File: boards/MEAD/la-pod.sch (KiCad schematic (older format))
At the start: 4 parts, among them J1 CONN_SFF8087

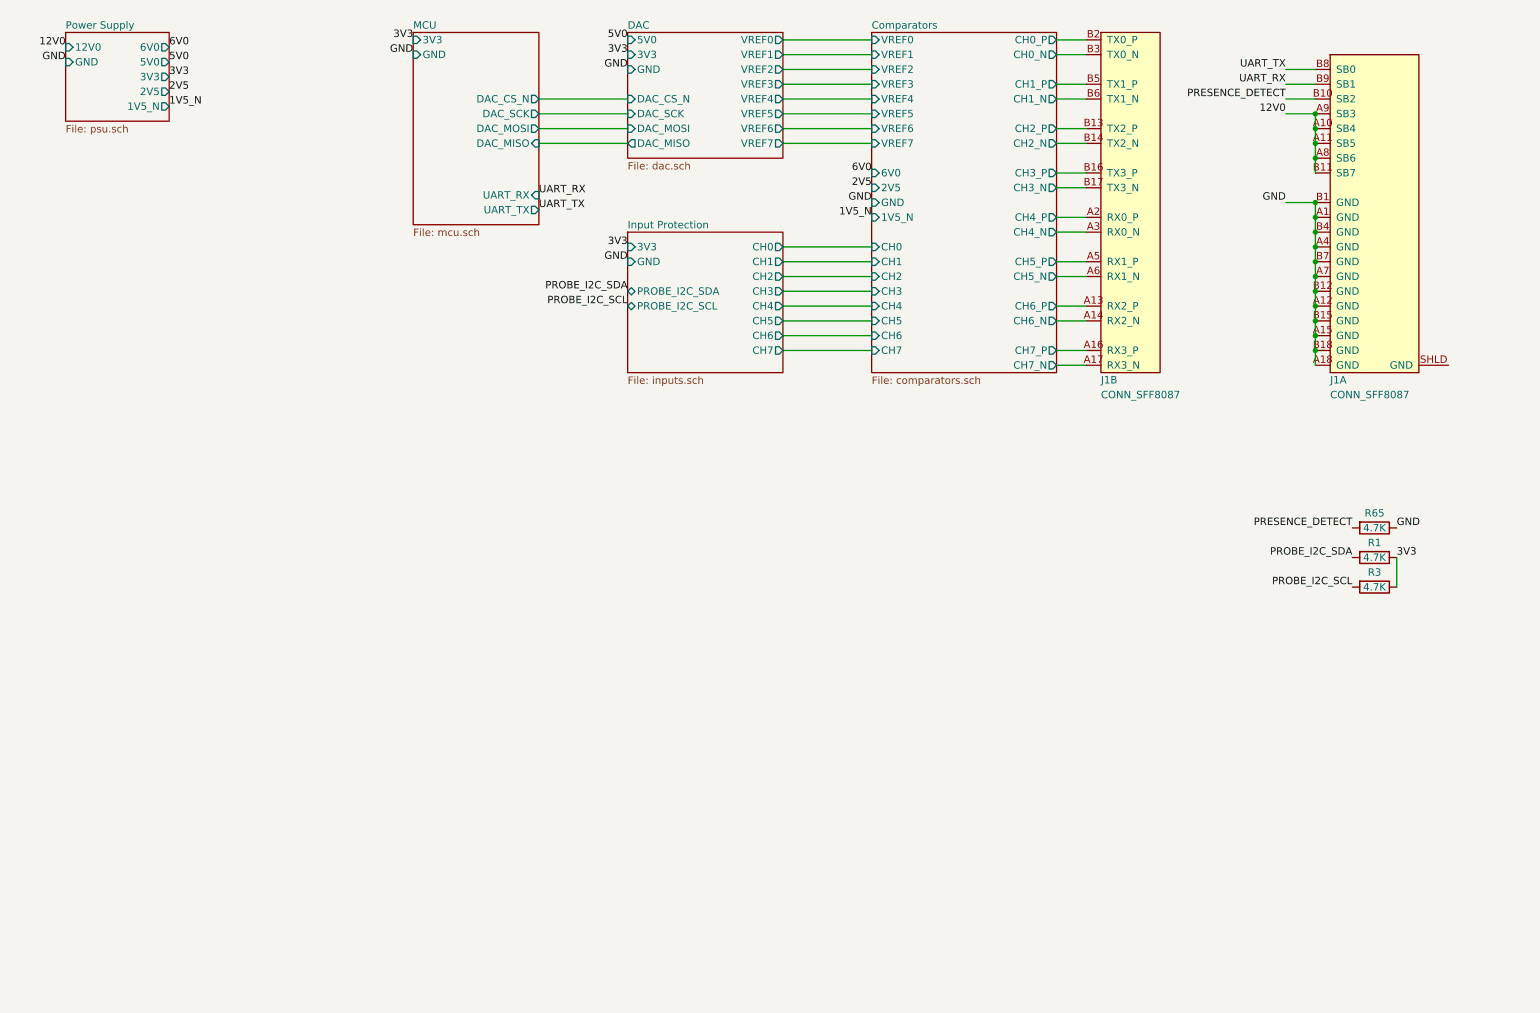
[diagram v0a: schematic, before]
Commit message: Updated MEAD LA pod design with display and different protection diodes
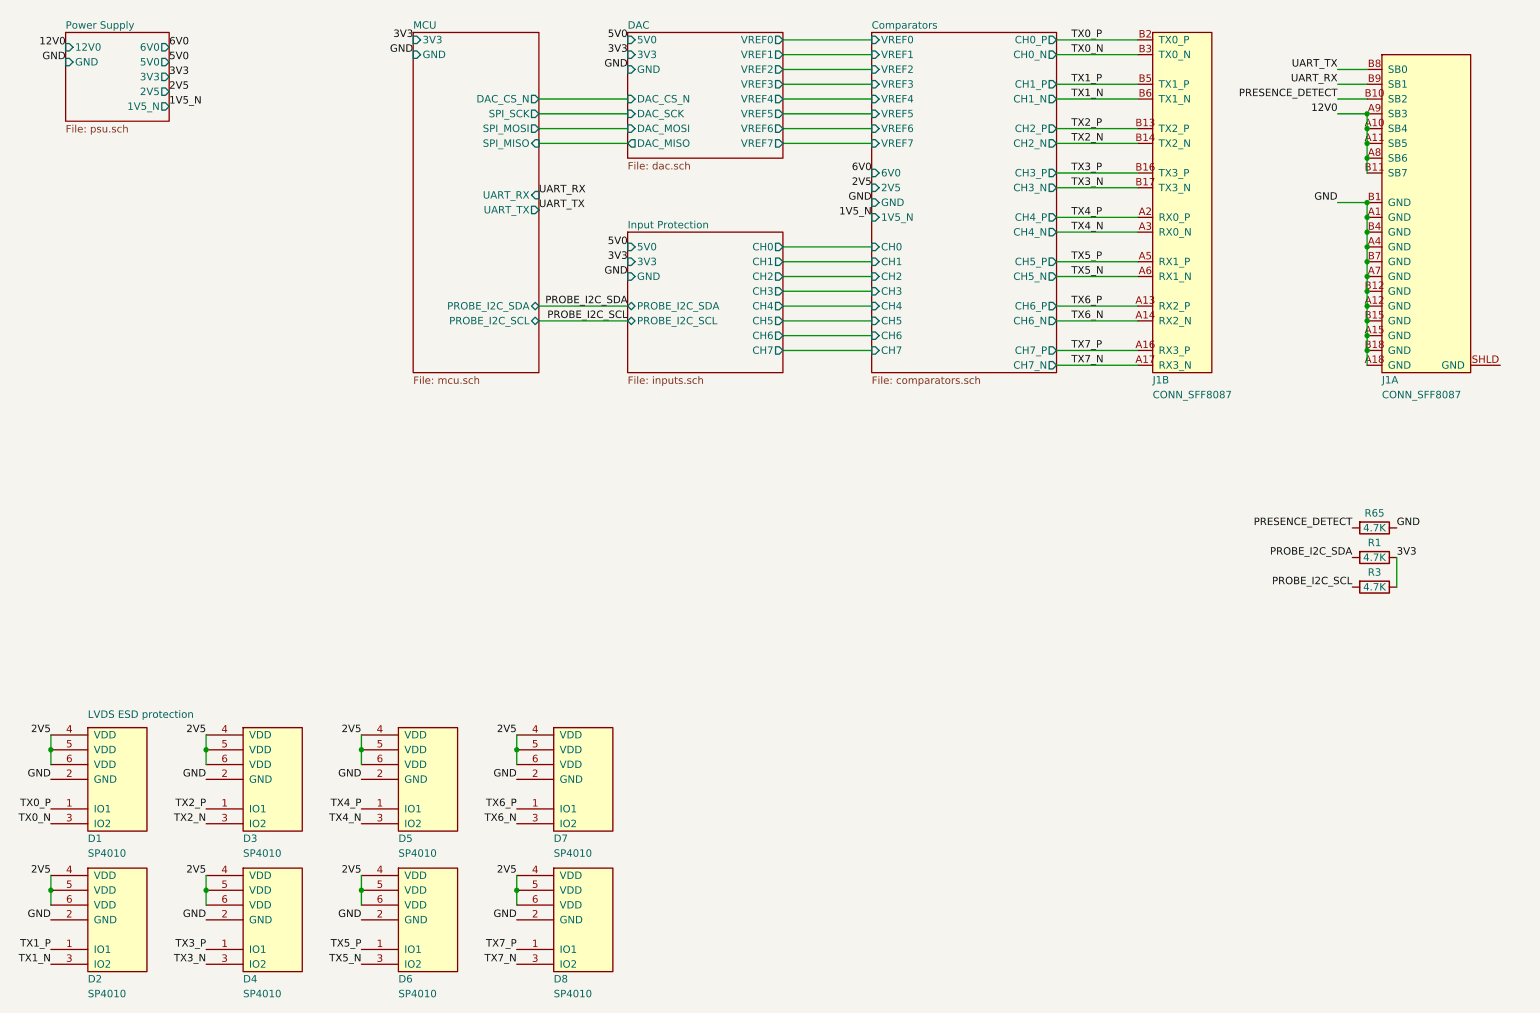
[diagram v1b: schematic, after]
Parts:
- added D1, D2, D3, D4, D5, D6, D7, D8: SP4010, symbol special-azonenberg:SP4010
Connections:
- net 2V5: now also D1.4 (VDD), D1.5 (VDD), D1.6 (VDD), D2.4 (VDD), D2.5 (VDD), D2.6 (VDD), D3.4 (VDD), D3.5 (VDD), D3.6 (VDD), D4.4 (VDD), D4.5 (VDD), D4.6 (VDD), D5.4 (VDD), D5.5 (VDD), D5.6 (VDD), D6.4 (VDD), D6.5 (VDD), D6.6 (VDD), D7.4 (VDD), D7.5 (VDD), D7.6 (VDD), D8.4 (VDD), D8.5 (VDD), D8.6 (VDD)
- net GND: now also D1.2 (GND), D2.2 (GND), D3.2 (GND), D4.2 (GND), D5.2 (GND), D6.2 (GND), D7.2 (GND), D8.2 (GND)
- net Comparators/CH0_N renamed TX0_N
- net TX0_N: now also D1.3 (IO2)
- net Comparators/CH0_P renamed TX0_P
- net TX0_P: now also D1.1 (IO1)
- net Comparators/CH1_N renamed TX1_N
- net TX1_N: now also D2.3 (IO2)
- net Comparators/CH1_P renamed TX1_P
- net TX1_P: now also D2.1 (IO1)
- net Comparators/CH2_N renamed TX2_N
- net TX2_N: now also D3.3 (IO2)
- net Comparators/CH2_P renamed TX2_P
- net TX2_P: now also D3.1 (IO1)
- net Comparators/CH3_N renamed TX3_N
- net TX3_N: now also D4.3 (IO2)
- net Comparators/CH3_P renamed TX3_P
- net TX3_P: now also D4.1 (IO1)
- net Comparators/CH4_N renamed TX4_N
- net TX4_N: now also D5.3 (IO2)
- net Comparators/CH4_P renamed TX4_P
- net TX4_P: now also D5.1 (IO1)
- net Comparators/CH5_N renamed TX5_N
- net TX5_N: now also D6.3 (IO2)
- net Comparators/CH5_P renamed TX5_P
- net TX5_P: now also D6.1 (IO1)
- net Comparators/CH6_N renamed TX6_N
- net TX6_N: now also D7.3 (IO2)
- net Comparators/CH6_P renamed TX6_P
- net TX6_P: now also D7.1 (IO1)
- net Comparators/CH7_N renamed TX7_N
- net TX7_N: now also D8.3 (IO2)
- net Comparators/CH7_P renamed TX7_P
- net TX7_P: now also D8.1 (IO1)
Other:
- note added: "LVDS ESD protection"
- moved on the sheet: J1A, J1B

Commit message: Updated LA pod schematic with additional ESD protection and noise filtering
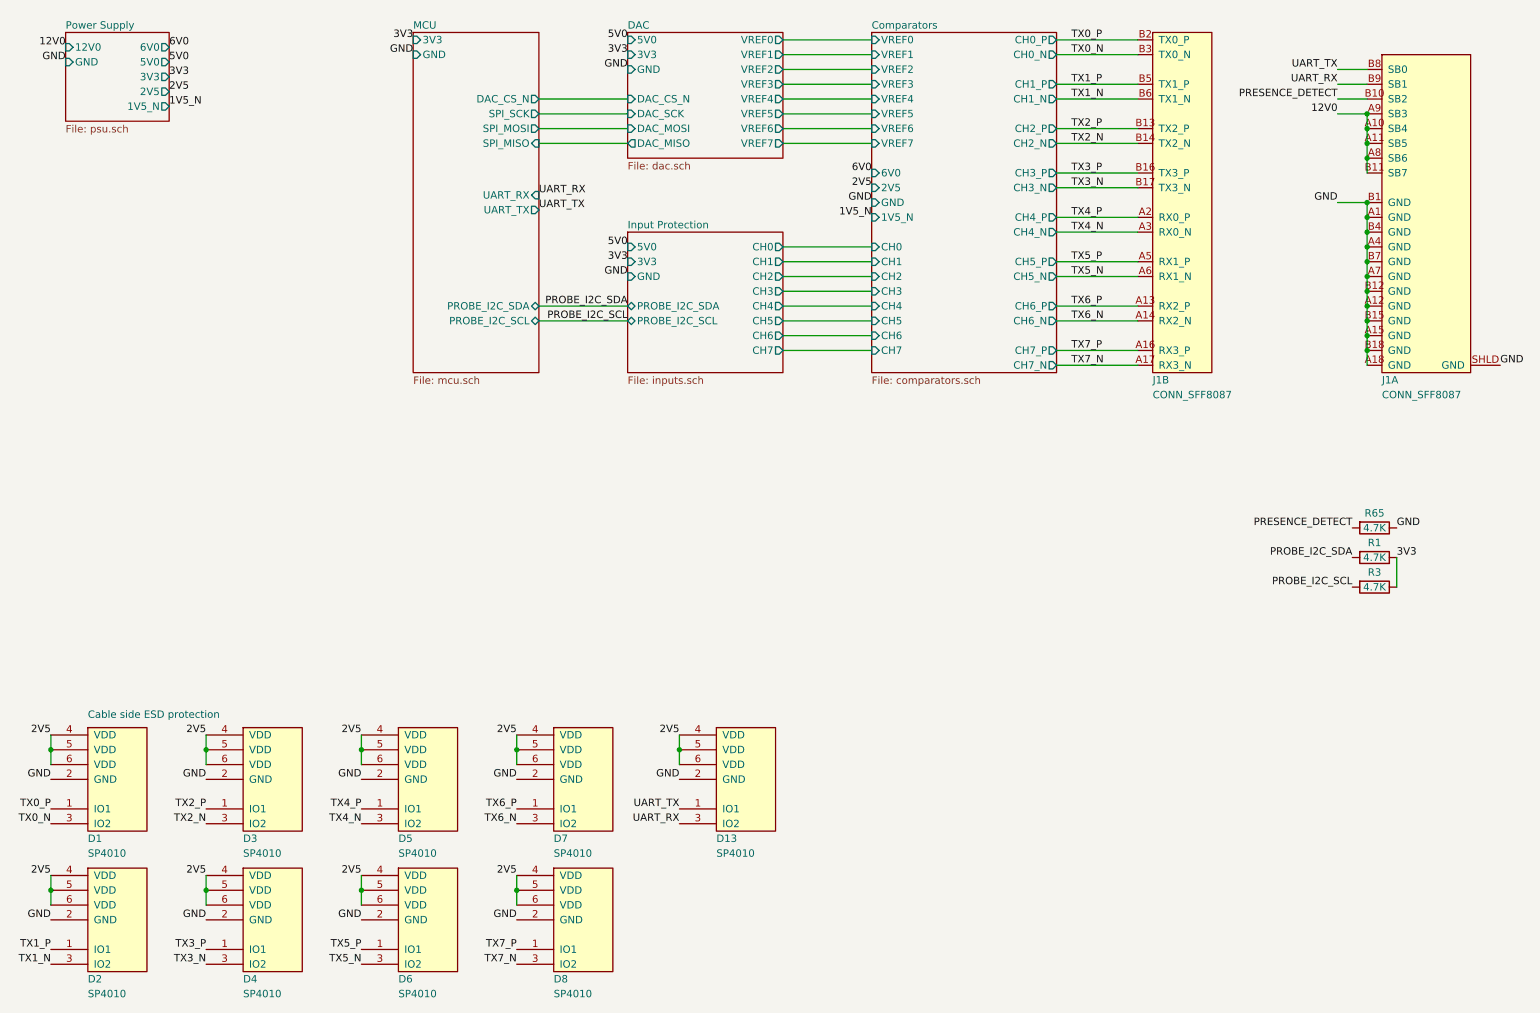
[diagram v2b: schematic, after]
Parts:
- added D13: SP4010, azonenberg_pcb:SOT23_6, symbol special-azonenberg:SP4010
- D1, D2, D3, D4, D5, D6, D7, D8: footprint (none) -> azonenberg_pcb:SOT23_6
- J1: footprint (none) -> azonenberg_pcb:CONN_SFF8087_MOLEX_75783-0140
- R1, R3, R65: footprint (none) -> azonenberg_pcb:EIA_0402_RES_NOSILK
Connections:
- net 2V5: now also D13.4 (VDD), D13.5 (VDD), D13.6 (VDD)
- net GND: now also J1.SHLD (GND), D13.2 (GND)
- net UART_RX: now also D13.3 (IO2)
- net UART_TX: now also D13.1 (IO1)
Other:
- note added: "Cable side ESD protection"
- note removed: "LVDS ESD protection"
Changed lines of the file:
@@
 F 0 "J1" H 9900 3400 50  0000 L CNN
 F 1 "CONN_SFF8087" H 9900 3300 50  0000 L CNN
-F 2 "" H 9900 3450 50  0001 C CNN
+F 2 "azonenberg_pcb:CONN_SFF8087_MOLEX_75783-0140" H 9900 3450 50  0001 C CNN
 F 3 "" H 9900 3450 50  0001 C CNN
 	1    9900 3450
@@
 F 0 "J1" H 8350 3400 50  0000 L CNN
 F 1 "CONN_SFF8087" H 8350 3300 50  0000 L CNN
-F 2 "" H 8350 3450 50  0001 C CNN
+F 2 "azonenberg_pcb:CONN_SFF8087_MOLEX_75783-0140" H 8350 3450 50  0001 C CNN
 F 3 "" H 8350 3450 50  0001 C CNN
 	2    8350 3450
@@
 F 0 "R65" V 9750 4500 50  0000 C CNN
 F 1 "4.7K" V 9850 4500 50  0000 C CNN
-F 2 "" V 9780 4500 50  0001 C CNN
+F 2 "azonenberg_pcb:EIA_0402_RES_NOSILK" V 9780 4500 50  0001 C CNN
 F 3 "" H 9850 4500 50  0001 C CNN
 	1    9850 4500
@@
 F 0 "R1" V 9750 4700 50  0000 C CNN
 F 1 "4.7K" V 9850 4700 50  0000 C CNN
-F 2 "" V 9780 4700 50  0001 C CNN
+F 2 "azonenberg_pcb:EIA_0402_RES_NOSILK" V 9780 4700 50  0001 C CNN
 F 3 "" H 9850 4700 50  0001 C CNN
 	1    9850 4700
@@
 F 0 "R3" V 9750 4900 50  0000 C CNN
 F 1 "4.7K" V 9850 4900 50  0000 C CNN
-F 2 "" V 9780 4900 50  0001 C CNN
+F 2 "azonenberg_pcb:EIA_0402_RES_NOSILK" V 9780 4900 50  0001 C CNN
 F 3 "" H 9850 4900 50  0001 C CNN
 	1    9850 4900
@@
 F 0 "D1" H 1150 6500 50  0000 L CNN
 F 1 "SP4010" H 1150 6400 50  0000 L CNN
-F 2 "" H 1150 6550 50  0001 C CNN
+F 2 "azonenberg_pcb:SOT23_6" H 1150 6550 50  0001 C CNN
 F 3 "" H 1150 6550 50  0001 C CNN
 	1    1150 6550
@@
 F 0 "D2" H 1150 7450 50  0000 L CNN
 F 1 "SP4010" H 1150 7350 50  0000 L CNN
-F 2 "" H 1150 7500 50  0001 C CNN
+F 2 "azonenberg_pcb:SOT23_6" H 1150 7500 50  0001 C CNN
 F 3 "" H 1150 7500 50  0001 C CNN
 	1    1150 7500
@@
 GND
 Text Notes 1150 5800 0    50   ~ 0
-LVDS ESD protection
+Cable side ESD protection
 $Comp
 L special-azonenberg:SP4010 D3
@@
 F 0 "D3" H 2200 6500 50  0000 L CNN
 F 1 "SP4010" H 2200 6400 50  0000 L CNN
-F 2 "" H 2200 6550 50  0001 C CNN
+F 2 "azonenberg_pcb:SOT23_6" H 2200 6550 50  0001 C CNN
 F 3 "" H 2200 6550 50  0001 C CNN
 	1    2200 6550
@@
 F 0 "D4" H 2200 7450 50  0000 L CNN
 F 1 "SP4010" H 2200 7350 50  0000 L CNN
-F 2 "" H 2200 7500 50  0001 C CNN
+F 2 "azonenberg_pcb:SOT23_6" H 2200 7500 50  0001 C CNN
 F 3 "" H 2200 7500 50  0001 C CNN
 	1    2200 7500
@@
 F 0 "D5" H 3250 6500 50  0000 L CNN
 F 1 "SP4010" H 3250 6400 50  0000 L CNN
-F 2 "" H 3250 6550 50  0001 C CNN
+F 2 "azonenberg_pcb:SOT23_6" H 3250 6550 50  0001 C CNN
 F 3 "" H 3250 6550 50  0001 C CNN
 	1    3250 6550
@@
 F 0 "D6" H 3250 7450 50  0000 L CNN
 F 1 "SP4010" H 3250 7350 50  0000 L CNN
-F 2 "" H 3250 7500 50  0001 C CNN
+F 2 "azonenberg_pcb:SOT23_6" H 3250 7500 50  0001 C CNN
 F 3 "" H 3250 7500 50  0001 C CNN
 	1    3250 7500
@@
 F 0 "D7" H 4300 6500 50  0000 L CNN
 F 1 "SP4010" H 4300 6400 50  0000 L CNN
-F 2 "" H 4300 6550 50  0001 C CNN
+F 2 "azonenberg_pcb:SOT23_6" H 4300 6550 50  0001 C CNN
 F 3 "" H 4300 6550 50  0001 C CNN
 	1    4300 6550
@@
 F 0 "D8" H 4300 7450 50  0000 L CNN
 F 1 "SP4010" H 4300 7350 50  0000 L CNN
-F 2 "" H 4300 7500 50  0001 C CNN
+F 2 "azonenberg_pcb:SOT23_6" H 4300 7500 50  0001 C CNN
 F 3 "" H 4300 7500 50  0001 C CNN
 	1    4300 7500
@@
 Wire Wire Line
 	4200 3100 4800 3100
+Text Label 10700 3400 0    50   ~ 0
+GND
+$Comp
+L special-azonenberg:SP4010 D13
+U 1 1 5ED20175
+P 5400 6550
+F 0 "D13" H 5400 6500 50  0000 L CNN
+F 1 "SP4010" H 5400 6400 50  0000 L CNN
+F 2 "azonenberg_pcb:SOT23_6" H 5400 6550 50  0001 C CNN
+F 3 "" H 5400 6550 50  0001 C CNN
+	1    5400 6550
+	1    0    0    -1
+$EndComp
+Text Label 5150 5900 2    50   ~ 0
+2V5
+Wire Wire Line
+	5150 5900 5150 6000
+Connection ~ 5150 6000
+Wire Wire Line
+	5150 6000 5150 6100
+Text Label 5150 6200 2    50   ~ 0
+GND
+Text Label 5150 6400 2    50   ~ 0
+UART_TX
+Text Label 5150 6500 2    50   ~ 0
+UART_RX
 $EndSCHEMATC

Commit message: MEAD: finished schematic review, added more test points
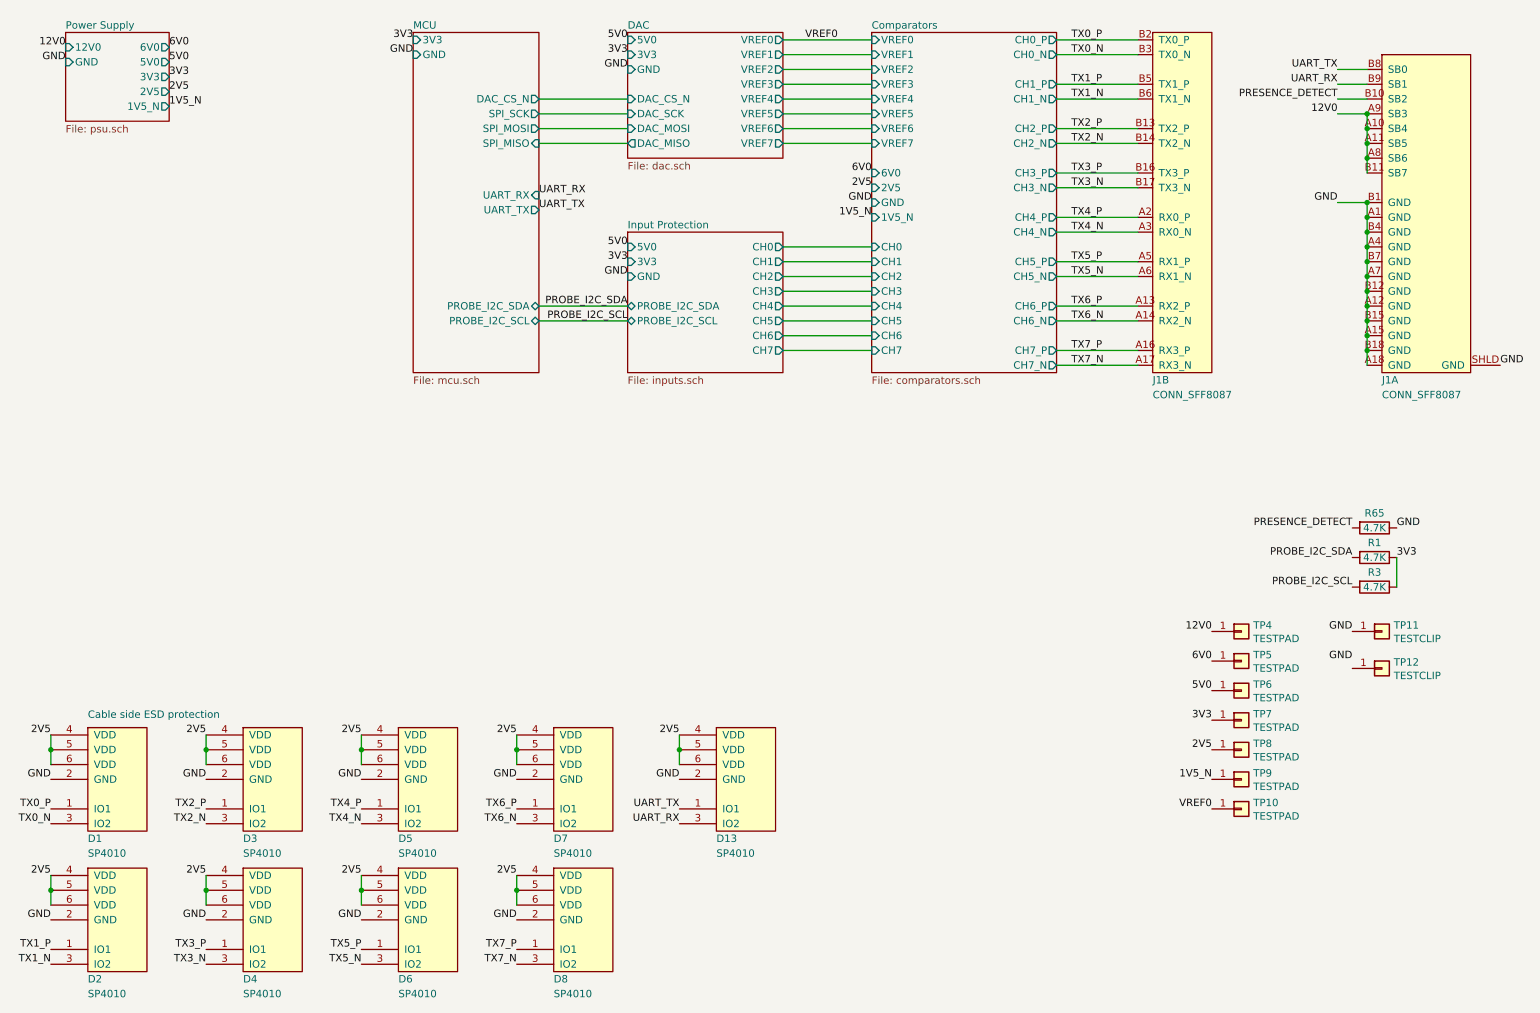
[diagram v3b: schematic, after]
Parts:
- added TP10, TP4, TP5, TP6, TP7, TP8, TP9: TESTPAD, azonenberg_pcb:TESTPOINT_SMT_0.5MM, symbol Connector:Conn_01x01
- added TP11, TP12: TESTCLIP, azonenberg_pcb:TESTPOINT_SMT_KEYSTONE_5016, symbol Connector:Conn_01x01
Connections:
- net 12V0: now also TP4.1 (Pin_1)
- net 1V5_N: now also TP9.1 (Pin_1)
- net 2V5: now also TP8.1 (Pin_1)
- net 3V3: now also TP7.1 (Pin_1)
- net 5V0: now also TP6.1 (Pin_1)
- net 6V0: now also TP5.1 (Pin_1)
- net GND: now also TP11.1 (Pin_1)
- new net VREF0: TP10.1 (Pin_1)
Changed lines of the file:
@@
 Sheet 1 6
 Title "Logic Analyzer Pod"
-Date "2020-05-28"
+Date "2020-05-29"
 Rev "0.1"
 Comp "Antikernel Labs"
@@
 Text Label 5150 6500 2    50   ~ 0
 UART_RX
+$Comp
+L Connector:Conn_01x01 TP11
+U 1 1 5ED596F2
+P 9900 5200
+F 0 "TP11" H 9980 5242 50  0000 L CNN
+F 1 "TESTCLIP" H 9980 5151 50  0000 L CNN
+F 2 "azonenberg_pcb:TESTPOINT_SMT_KEYSTONE_5016" H 9900 5200 50  0001 C CNN
+F 3 "~" H 9900 5200 50  0001 C CNN
+	1    9900 5200
+	1    0    0    -1
+$EndComp
+Text Label 9700 5200 2    50   ~ 0
+GND
+$Comp
+L Connector:Conn_01x01 TP12
+U 1 1 5ED5A23C
+P 9900 5450
+F 0 "TP12" H 9980 5492 50  0000 L CNN
+F 1 "TESTCLIP" H 9980 5401 50  0000 L CNN
+F 2 "azonenberg_pcb:TESTPOINT_SMT_KEYSTONE_5016" H 9900 5450 50  0001 C CNN
+F 3 "~" H 9900 5450 50  0001 C CNN
+	1    9900 5450
+	1    0    0    -1
+$EndComp
+Text Label 9700 5400 2    50   ~ 0
+GND
+$Comp
+L Connector:Conn_01x01 TP4
+U 1 1 5ED5A825
+P 8950 5200
+F 0 "TP4" H 9030 5242 50  0000 L CNN
+F 1 "TESTPAD" H 9030 5151 50  0000 L CNN
+F 2 "azonenberg_pcb:TESTPOINT_SMT_0.5MM" H 8950 5200 50  0001 C CNN
+F 3 "~" H 8950 5200 50  0001 C CNN
+	1    8950 5200
+	1    0    0    -1
+$EndComp
+Text Label 8750 5200 2    50   ~ 0
+12V0
+$Comp
+L Connector:Conn_01x01 TP5
+U 1 1 5ED5B185
+P 8950 5400
+F 0 "TP5" H 9030 5442 50  0000 L CNN
+F 1 "TESTPAD" H 9030 5351 50  0000 L CNN
+F 2 "azonenberg_pcb:TESTPOINT_SMT_0.5MM" H 8950 5400 50  0001 C CNN
+F 3 "~" H 8950 5400 50  0001 C CNN
+	1    8950 5400
+	1    0    0    -1
+$EndComp
+Text Label 8750 5400 2    50   ~ 0
+6V0
+$Comp
+L Connector:Conn_01x01 TP6
+U 1 1 5ED5B641
+P 8950 5600
+F 0 "TP6" H 9030 5642 50  0000 L CNN
+F 1 "TESTPAD" H 9030 5551 50  0000 L CNN
+F 2 "azonenberg_pcb:TESTPOINT_SMT_0.5MM" H 8950 5600 50  0001 C CNN
+F 3 "~" H 8950 5600 50  0001 C CNN
+	1    8950 5600
+	1    0    0    -1
+$EndComp
+Text Label 8750 5600 2    50   ~ 0
+5V0
+$Comp
+L Connector:Conn_01x01 TP7
+U 1 1 5ED5BCF0
+P 8950 5800
+F 0 "TP7" H 9030 5842 50  0000 L CNN
+F 1 "TESTPAD" H 9030 5751 50  0000 L CNN
+F 2 "azonenberg_pcb:TESTPOINT_SMT_0.5MM" H 8950 5800 50  0001 C CNN
+F 3 "~" H 8950 5800 50  0001 C CNN
+	1    8950 5800
+	1    0    0    -1
+$EndComp
+Text Label 8750 5800 2    50   ~ 0
+3V3
+$Comp
+L Connector:Conn_01x01 TP8
+U 1 1 5ED5C198
+P 8950 6000
+F 0 "TP8" H 9030 6042 50  0000 L CNN
+F 1 "TESTPAD" H 9030 5951 50  0000 L CNN
+F 2 "azonenberg_pcb:TESTPOINT_SMT_0.5MM" H 8950 6000 50  0001 C CNN
+F 3 "~" H 8950 6000 50  0001 C CNN
+	1    8950 6000
+	1    0    0    -1
+$EndComp
+Text Label 8750 6000 2    50   ~ 0
+2V5
+$Comp
+L Connector:Conn_01x01 TP9
+U 1 1 5ED5C910
+P 8950 6200
+F 0 "TP9" H 9030 6242 50  0000 L CNN
+F 1 "TESTPAD" H 9030 6151 50  0000 L CNN
+F 2 "azonenberg_pcb:TESTPOINT_SMT_0.5MM" H 8950 6200 50  0001 C CNN
+F 3 "~" H 8950 6200 50  0001 C CNN
+	1    8950 6200
+	1    0    0    -1
+$EndComp
+Text Label 8750 6200 2    50   ~ 0
+1V5_N
+Text Label 6000 1200 0    50   ~ 0
+VREF0
+Text Label 8750 6400 2    50   ~ 0
+VREF0
+$Comp
+L Connector:Conn_01x01 TP10
+U 1 1 5ED5D15E
+P 8950 6400
+F 0 "TP10" H 9030 6442 50  0000 L CNN
+F 1 "TESTPAD" H 9030 6351 50  0000 L CNN
+F 2 "azonenberg_pcb:TESTPOINT_SMT_0.5MM" H 8950 6400 50  0001 C CNN
+F 3 "~" H 8950 6400 50  0001 C CNN
+	1    8950 6400
+	1    0    0    -1
+$EndComp
 $EndSCHEMATC
